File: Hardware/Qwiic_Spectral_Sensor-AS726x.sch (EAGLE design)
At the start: 28 parts, among them J2 Serial Interface, J5 Flash Programming, U1 AS726X, U3 4MB Flash

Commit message: Updated LED
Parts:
- added LOGO2: SFE_LOGO_FLAME.2_INCH, SparkFun-Aesthetics:SFE_LOGO_FLAME.2_INCH
- D2: value 5700k -> White, 60mA; device SparkX:LEDLD -> SparkFun-LED:LED-WHITE3014
- LOGO1: value SFE_LOGO_NAME_FLAME.1_INCH -> SFE_LOGO_FLAME.2_INCH; device SparkFun-Aesthetics:SFE_LOGO_NAME_FLAME.1_INCH -> SparkFun-Aesthetics:SFE_LOGO_FLAME.2_INCH
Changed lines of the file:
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@@
 <layer number="230" name="230bmp" color="7" fill="1" visible="yes" active="yes"/>
 <layer number="231" name="231bmp" color="7" fill="1" visible="yes" active="yes"/>
+<layer number="232" name="Eagle3D_PG2" color="7" fill="1" visible="yes" active="yes"/>
+<layer number="233" name="Eagle3D_PG3" color="7" fill="1" visible="yes" active="yes"/>
 <layer number="248" name="Housing" color="7" fill="1" visible="yes" active="yes"/>
 <layer number="249" name="Edge" color="7" fill="1" visible="yes" active="yes"/>
@@
 <part name="GND8" library="SparkFun-PowerSymbols" deviceset="GND" device=""/>
 <part name="SUPPLY13" library="SparkFun-PowerSymbols" deviceset="3.3V" device=""/>
-<part name="D2" library="SparkX" deviceset="LED" device="LD" value="5700k"/>
+<part name="D2" library="SparkFun-LED" deviceset="LED-WHITE" device="3014" value="White, 60mA"/>
 <part name="J5" library="SparkFun-Connectors" deviceset="AVR_SPI_PROG_3X2" device="TESTPOINTS" value="Flash Programming"/>
 <part name="SUPPLY14" library="SparkFun-PowerSymbols" deviceset="3.3V" device=""/>
@@
 <part name="D4" library="SparkX" deviceset="LED" device="NS" value="Incandescent"/>
 <part name="JP4" library="SparkFun-Jumpers" deviceset="JUMPER-SMT_2_NC_PASTE" device="_NO-SILK" value=""/>
-<part name="LOGO1" library="SparkFun-Aesthetics" deviceset="SFE_LOGO_NAME_FLAME" device=".1_INCH"/>
+<part name="LOGO1" library="SparkFun-Aesthetics" deviceset="SFE_LOGO_FLAME" device=".2_INCH"/>
+<part name="LOGO2" library="SparkFun-Aesthetics" deviceset="SFE_LOGO_FLAME" device=".2_INCH"/>
 </parts>
 <sheets>
@@
 <instance part="GND8" gate="1" x="116.84" y="43.18" rot="MR0"/>
 <instance part="SUPPLY13" gate="G$1" x="116.84" y="58.42" rot="MR0"/>
-<instance part="D2" gate="D1" x="40.64" y="144.78" smashed="yes">
+<instance part="D2" gate="G$1" x="40.64" y="144.78" smashed="yes">
 <attribute name="NAME" x="40.132" y="138.176" size="1.778" layer="95" font="vector" rot="R90"/>
 <attribute name="VALUE" x="42.418" y="139.192" size="1.778" layer="96" font="vector" rot="R90" align="top-left"/>
@@
 </instance>
 <instance part="JP4" gate="G$1" x="40.64" y="154.94" rot="R90"/>
-<instance part="LOGO1" gate="G$1" x="88.9" y="2.54"/>
+<instance part="LOGO1" gate="G$1" x="134.62" y="5.08"/>
+<instance part="LOGO2" gate="G$1" x="134.62" y="5.08"/>
 </instances>
 <busses>
@@
 <wire x1="60.96" y1="132.08" x2="40.64" y2="132.08" width="0.1524" layer="91"/>
 <wire x1="40.64" y1="132.08" x2="40.64" y2="139.7" width="0.1524" layer="91"/>
-<pinref part="D2" gate="D1" pin="C"/>
+<pinref part="D2" gate="G$1" pin="C"/>
 <wire x1="33.02" y1="139.7" x2="33.02" y2="132.08" width="0.1524" layer="91"/>
 <wire x1="33.02" y1="132.08" x2="40.64" y2="132.08" width="0.1524" layer="91"/>
@@
 <net name="N$6" class="0">
 <segment>
-<pinref part="D2" gate="D1" pin="A"/>
+<pinref part="D2" gate="G$1" pin="A"/>
 <pinref part="JP4" gate="G$1" pin="1"/>
 <wire x1="40.64" y1="149.86" x2="40.64" y2="147.32" width="0.1524" layer="91"/>

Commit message: Added LED, I2C connectors to SFE library and changed components in schematic
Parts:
- J1, J4: value (none) -> Qwiic Right Angle; device SparkX:I2C_STANDARDJS-1MM -> SparkFun-Connectors:I2C_STANDARDQWIIC
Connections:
- net 3.3V: now also J1.2, J4.2; no longer J1.VCC, J4.VCC
- net GND: now also J1.1, J4.1; no longer J1.GND, J4.GND
- net RX/SCL: now also J1.4, J4.4; no longer J1.SCL, J4.SCL
- net TX/SDA: now also J1.3, J4.3; no longer J1.SDA, J4.SDA
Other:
- note added: "U1 can be populated with AS7262 or AS7263"
- note removed: "FTDI Port"
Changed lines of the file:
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@@
 <part name="SUPPLY6" library="SparkFun-PowerSymbols" deviceset="3.3V" device=""/>
 <part name="GND5" library="SparkFun-PowerSymbols" deviceset="GND" device=""/>
-<part name="J1" library="SparkX" deviceset="I2C_STANDARD" device="JS-1MM"/>
+<part name="J1" library="SparkFun-Connectors" deviceset="I2C_STANDARD" device="QWIIC" value="Qwiic Right Angle"/>
 <part name="SUPPLY7" library="SparkFun-PowerSymbols" deviceset="3.3V" device=""/>
 <part name="D1" library="SparkFun-LED" deviceset="LED-BLUE" device="0603" value="BLUE"/>
@@
 <part name="SUPPLY3" library="SparkFun-PowerSymbols" deviceset="3.3V" device=""/>
 <part name="GND3" library="SparkFun-PowerSymbols" deviceset="GND" device=""/>
-<part name="J4" library="SparkX" deviceset="I2C_STANDARD" device="JS-1MM"/>
+<part name="J4" library="SparkFun-Connectors" deviceset="I2C_STANDARD" device="QWIIC" value="Qwiic Right Angle"/>
 <part name="GND8" library="SparkFun-PowerSymbols" deviceset="GND" device=""/>
 <part name="SUPPLY13" library="SparkFun-PowerSymbols" deviceset="3.3V" device=""/>
@@
 <text x="10.16" y="116.84" size="1.778" layer="97">CRI: 80</text>
 <text x="48.26" y="81.28" size="1.778" layer="97">7-bit unshifted I2C address: 0x49</text>
-<text x="134.62" y="45.72" size="1.778" layer="91" rot="R90">FTDI Port</text>
-<text x="180.34" y="45.72" size="1.778" layer="91" rot="R90">FTDI Port</text>
 <text x="93.98" y="43.18" size="1.778" layer="91" rot="R90">I2C interface</text>
 <text x="93.98" y="27.94" size="1.778" layer="91" rot="R90">Interrupt/
 Reset</text>
 <text x="148.59" y="7.112" size="2.54" layer="95">Revised by: Andy England</text>
+<text x="48.26" y="106.68" size="1.524" layer="91">U1 can be populated with AS7262 or AS7263</text>
 </plain>
 <instances>
@@
 <instance part="SUPPLY6" gate="G$1" x="205.74" y="152.4"/>
 <instance part="GND5" gate="1" x="170.18" y="137.16"/>
-<instance part="J1" gate="G$1" x="172.72" y="50.8" rot="MR0"/>
+<instance part="J1" gate="G$1" x="172.72" y="50.8" smashed="yes" rot="MR0">
+<attribute name="VALUE" x="180.594" y="63.5" size="1.778" layer="96" font="vector" rot="MR270" align="top-left"/>
+<attribute name="NAME" x="177.8" y="58.674" size="1.778" layer="95" font="vector" rot="MR0"/>
+</instance>
 <instance part="SUPPLY7" gate="G$1" x="170.18" y="152.4"/>
 <instance part="D1" gate="G$1" x="50.8" y="144.78" smashed="yes">
@@
 <instance part="SUPPLY3" gate="G$1" x="215.9" y="63.5" rot="MR0"/>
 <instance part="GND3" gate="1" x="215.9" y="43.18" rot="MR0"/>
-<instance part="J4" gate="G$1" x="127" y="50.8" rot="MR0"/>
+<instance part="J4" gate="G$1" x="127" y="50.8" smashed="yes" rot="MR0">
+<attribute name="VALUE" x="134.874" y="63.5" size="1.778" layer="96" font="vector" rot="MR270" align="top-left"/>
+<attribute name="NAME" x="132.08" y="58.674" size="1.778" layer="95" font="vector" rot="MR0"/>
+</instance>
 <instance part="GND8" gate="1" x="116.84" y="43.18" rot="MR0"/>
 <instance part="SUPPLY13" gate="G$1" x="116.84" y="58.42" rot="MR0"/>
@@
 </segment>
 <segment>
-<pinref part="J1" gate="G$1" pin="GND"/>
+<pinref part="J1" gate="G$1" pin="1"/>
 <wire x1="165.1" y1="48.26" x2="162.56" y2="48.26" width="0.1524" layer="91"/>
 <wire x1="162.56" y1="48.26" x2="162.56" y2="45.72" width="0.1524" layer="91"/>
@@
 </segment>
 <segment>
-<pinref part="J4" gate="G$1" pin="GND"/>
+<pinref part="J4" gate="G$1" pin="1"/>
 <wire x1="119.38" y1="48.26" x2="116.84" y2="48.26" width="0.1524" layer="91"/>
 <wire x1="116.84" y1="48.26" x2="116.84" y2="45.72" width="0.1524" layer="91"/>
@@
 </segment>
 <segment>
-<pinref part="J1" gate="G$1" pin="SCL"/>
+<pinref part="J1" gate="G$1" pin="4"/>
 <wire x1="165.1" y1="55.88" x2="160.02" y2="55.88" width="0.1524" layer="91"/>
 <label x="160.02" y="55.88" size="1.27" layer="95" rot="R180" xref="yes"/>
@@
 </segment>
 <segment>
-<pinref part="J4" gate="G$1" pin="SCL"/>
+<pinref part="J4" gate="G$1" pin="4"/>
 <wire x1="119.38" y1="55.88" x2="114.3" y2="55.88" width="0.1524" layer="91"/>
 <label x="114.3" y="55.88" size="1.27" layer="95" rot="R180" xref="yes"/>
@@
 </segment>
 <segment>
-<pinref part="J1" gate="G$1" pin="SDA"/>
+<pinref part="J1" gate="G$1" pin="3"/>
 <wire x1="165.1" y1="53.34" x2="160.02" y2="53.34" width="0.1524" layer="91"/>
 <label x="160.02" y="53.34" size="1.27" layer="95" rot="R180" xref="yes"/>
@@
 </segment>
 <segment>
-<pinref part="J4" gate="G$1" pin="SDA"/>
+<pinref part="J4" gate="G$1" pin="3"/>
 <wire x1="119.38" y1="53.34" x2="114.3" y2="53.34" width="0.1524" layer="91"/>
 <label x="114.3" y="53.34" size="1.27" layer="95" rot="R180" xref="yes"/>
@@
 </segment>
 <segment>
-<pinref part="J1" gate="G$1" pin="VCC"/>
+<pinref part="J1" gate="G$1" pin="2"/>
 <wire x1="165.1" y1="50.8" x2="162.56" y2="50.8" width="0.1524" layer="91"/>
 <wire x1="162.56" y1="50.8" x2="162.56" y2="58.42" width="0.1524" layer="91"/>
@@
 </segment>
 <segment>
-<pinref part="J4" gate="G$1" pin="VCC"/>
+<pinref part="J4" gate="G$1" pin="2"/>
 <wire x1="119.38" y1="50.8" x2="116.84" y2="50.8" width="0.1524" layer="91"/>
 <wire x1="116.84" y1="50.8" x2="116.84" y2="58.42" width="0.1524" layer="91"/>

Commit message: Updated all schematics to point to proper library
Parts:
- U1: value AS726X -> IR; device SparkX:AS726X -> SparkFun-Sensors:AS726XIR
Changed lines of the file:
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@@
 <part name="FD1" library="SparkFun-Aesthetics" deviceset="FIDUCIAL" device="1X2"/>
 <part name="FD2" library="SparkFun-Aesthetics" deviceset="FIDUCIAL" device="1X2"/>
-<part name="U1" library="SparkX" deviceset="AS726X" device=""/>
+<part name="U1" library="SparkFun-Sensors" deviceset="AS726X" device="IR" value="IR"/>
 <part name="GND2" library="SparkFun-PowerSymbols" deviceset="GND" device=""/>
 <part name="SUPPLY1" library="SparkFun-PowerSymbols" deviceset="3.3V" device=""/>

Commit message: Fixed minor borad layout issues
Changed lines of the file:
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@@
 Reset</text>
 <text x="148.59" y="7.112" size="2.54" layer="95">Revised by: Andy England</text>
-<text x="48.26" y="106.68" size="1.524" layer="91">U1 can be populated with AS7262 or AS7263</text>
+<text x="48.26" y="106.68" size="1.524" layer="97">U1 can be populated with AS7262 or AS7263</text>
 </plain>
 <instances>

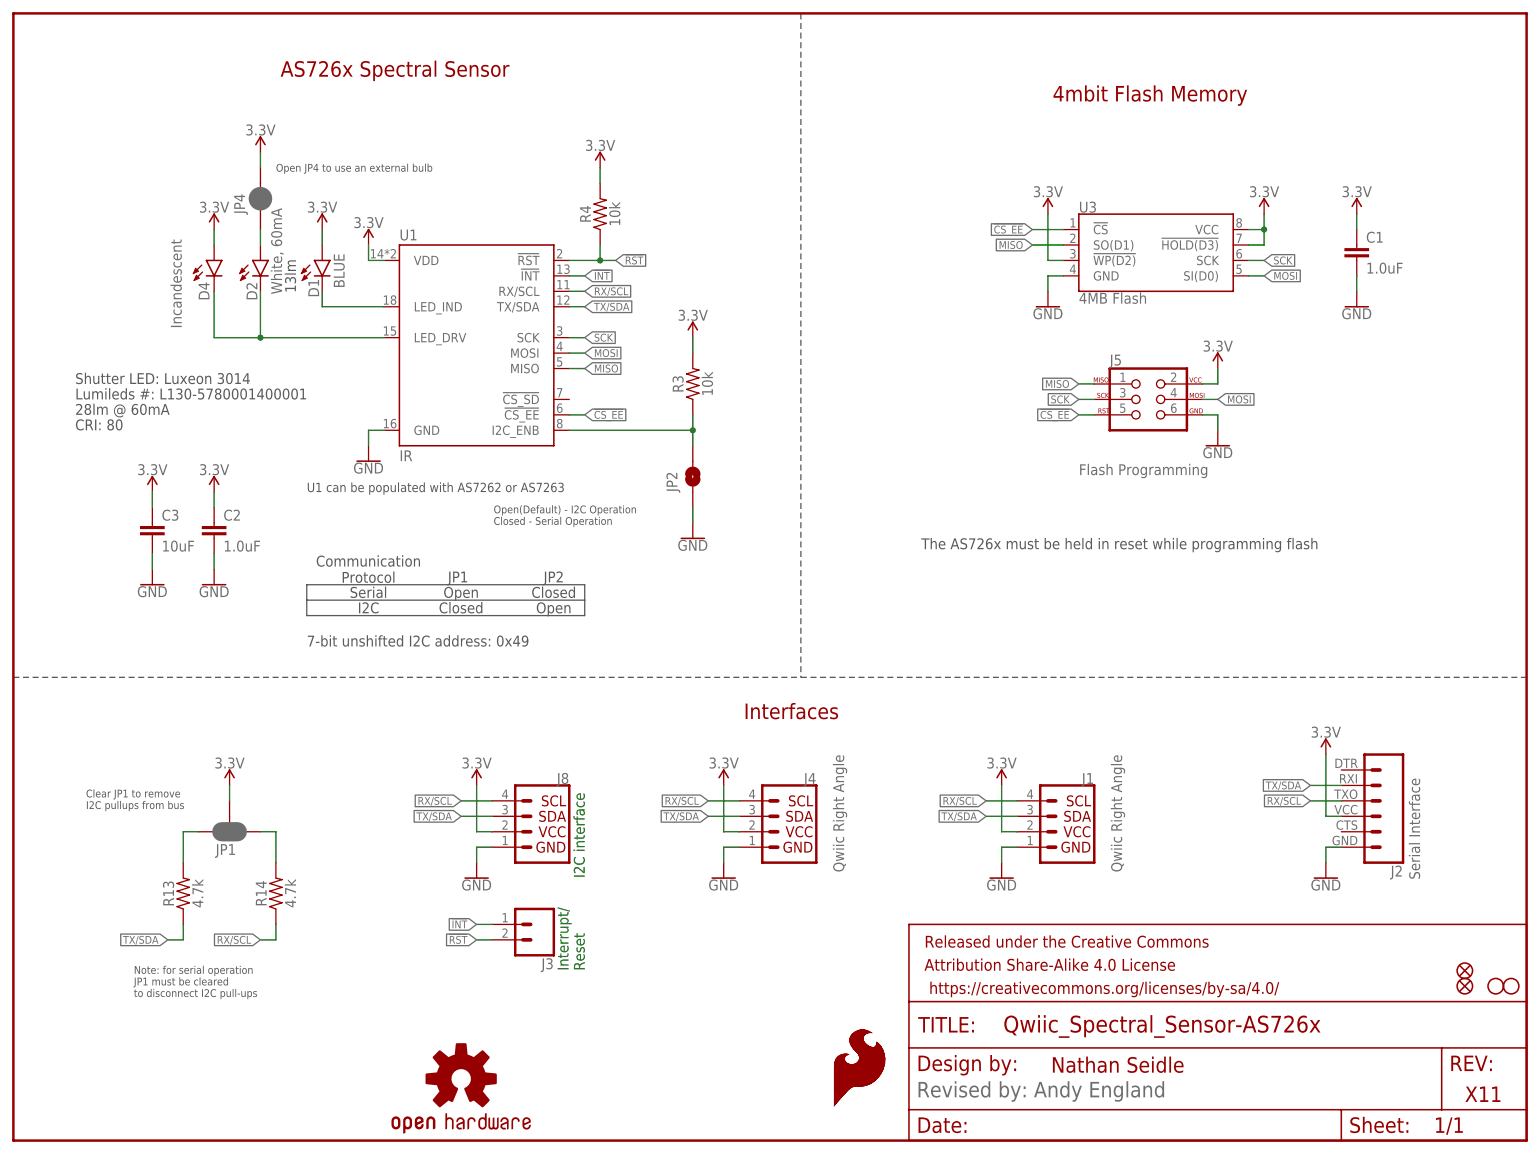
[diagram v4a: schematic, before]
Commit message: Post design review changes. Cream on JP1 and AS726X still needs to be changed
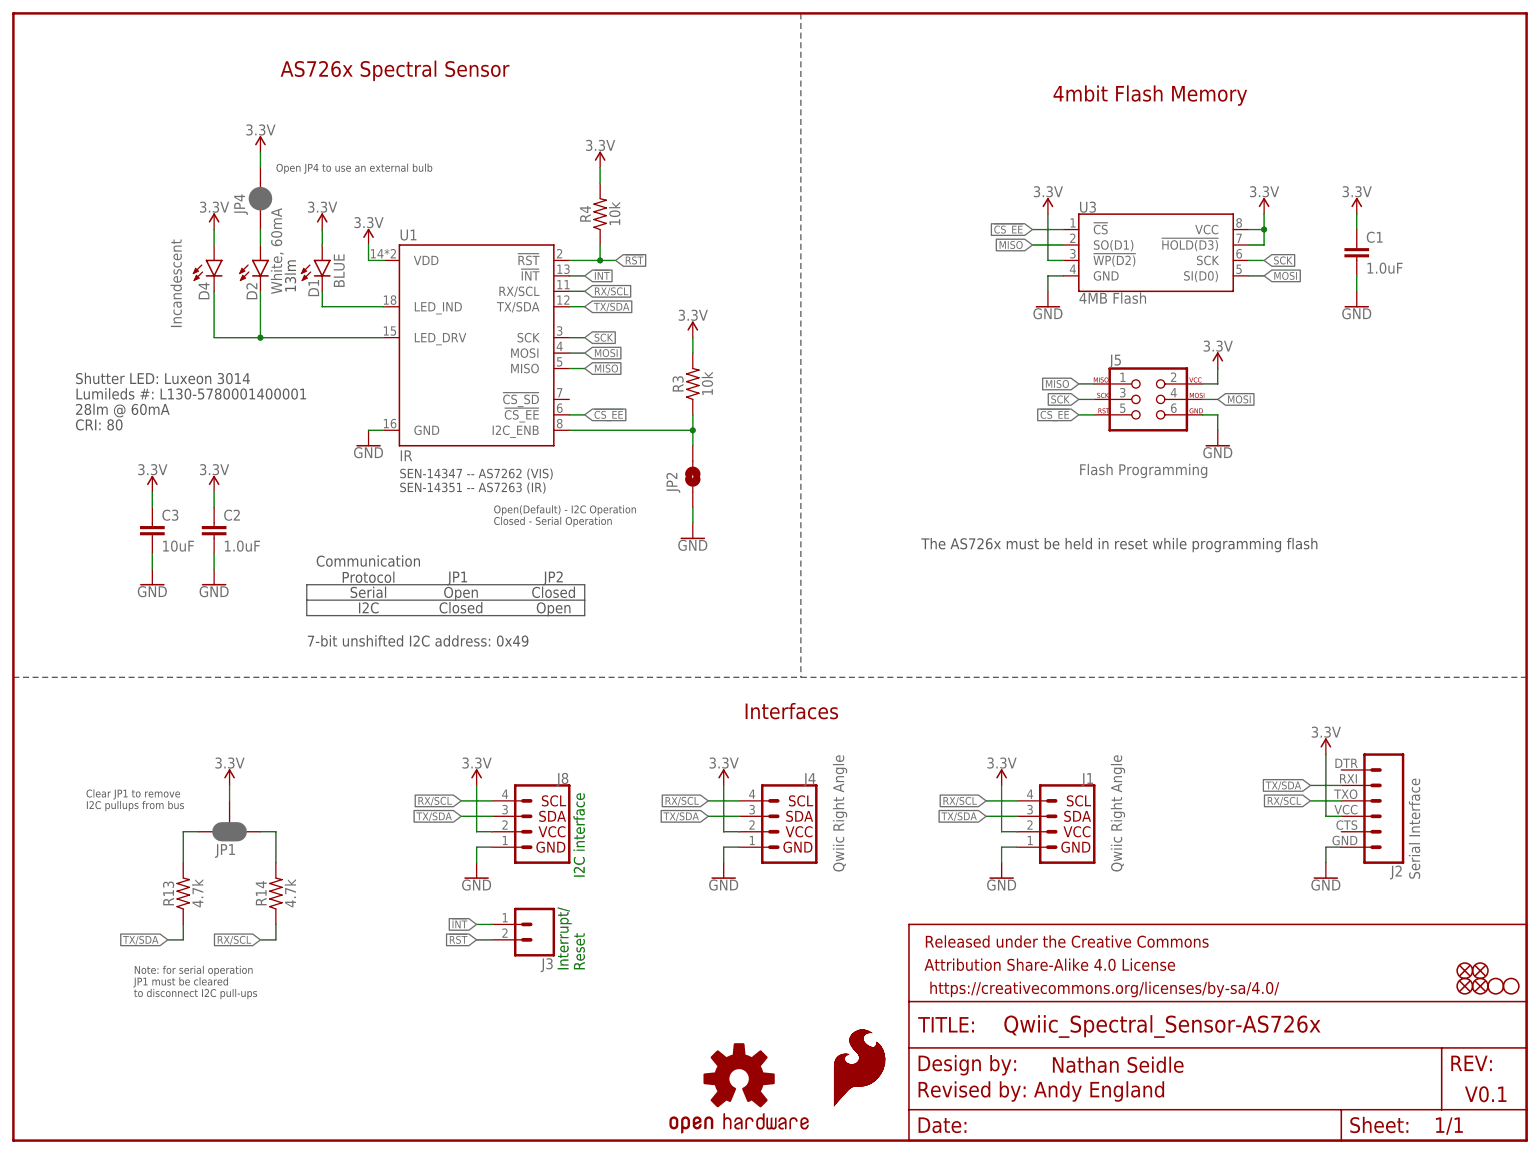
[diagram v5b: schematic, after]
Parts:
- added FD3, FD4: FIDUCIAL1X2, SparkFun-Aesthetics:FIDUCIAL1X2
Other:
- note added: "SEN-14347 -- AS7262 (VIS) SEN-14351 -- AS7263 (IR)"
- note added: "V0.1"
- note removed: "U1 can be populated with AS7262 or AS7263"
- note removed: "X11"
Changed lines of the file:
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@@
 <part name="LOGO1" library="SparkFun-Aesthetics" deviceset="SFE_LOGO_FLAME" device=".2_INCH"/>
 <part name="LOGO2" library="SparkFun-Aesthetics" deviceset="SFE_LOGO_FLAME" device=".2_INCH"/>
+<part name="FD3" library="SparkFun-Aesthetics" deviceset="FIDUCIAL" device="1X2"/>
+<part name="FD4" library="SparkFun-Aesthetics" deviceset="FIDUCIAL" device="1X2"/>
 </parts>
 <sheets>
@@
 <text x="11.938" y="56.134" size="1.27" layer="97" rot="R180" align="center-right">Clear JP1 to remove
 I2C pullups from bus</text>
-<text x="238.76" y="7.62" size="2.54" layer="94" align="center-left">X11</text>
+<text x="238.76" y="7.62" size="2.54" layer="94" align="center-left">V0.1</text>
 <text x="170.688" y="12.446" size="2.54" layer="94" align="center-left">Nathan Seidle</text>
 <wire x1="0" y1="76.2" x2="129.54" y2="76.2" width="0.2032" layer="97" style="longdash"/>
@@
 <text x="93.98" y="27.94" size="1.778" layer="91" rot="R90">Interrupt/
 Reset</text>
-<text x="148.59" y="7.112" size="2.54" layer="95">Revised by: Andy England</text>
-<text x="48.26" y="106.68" size="1.524" layer="97">U1 can be populated with AS7262 or AS7263</text>
+<text x="148.59" y="7.112" size="2.54" layer="94">Revised by: Andy England</text>
+<text x="63.5" y="106.68" size="1.524" layer="97">SEN-14347 -- AS7262 (VIS)
+SEN-14351 -- AS7263 (IR)</text>
 </plain>
 <instances>
@@
 <attribute name="VALUE" x="35.179" y="48.26" size="1.778" layer="96" font="vector" rot="R270" align="top-left"/>
 </instance>
-<instance part="LOGO4" gate="G$1" x="73.66" y="10.16"/>
+<instance part="LOGO4" gate="G$1" x="119.38" y="10.16"/>
 <instance part="FD1" gate="G$1" x="238.76" y="25.4"/>
 <instance part="FD2" gate="G$1" x="238.76" y="27.94"/>
 <instance part="U1" gate="U1" x="76.2" y="129.54"/>
-<instance part="GND2" gate="1" x="58.42" y="111.76"/>
+<instance part="GND2" gate="1" x="58.42" y="114.3"/>
 <instance part="SUPPLY1" gate="G$1" x="58.42" y="147.32"/>
 <instance part="R3" gate="G$1" x="111.76" y="124.46" rot="R90"/>
@@
 <instance part="LOGO1" gate="G$1" x="134.62" y="5.08"/>
 <instance part="LOGO2" gate="G$1" x="134.62" y="5.08"/>
+<instance part="FD3" gate="G$1" x="241.3" y="27.94"/>
+<instance part="FD4" gate="G$1" x="241.3" y="25.4"/>
 </instances>
 <busses>
@@
 <pinref part="U1" gate="U1" pin="GND"/>
 <wire x1="60.96" y1="116.84" x2="58.42" y2="116.84" width="0.1524" layer="91"/>
-<wire x1="58.42" y1="116.84" x2="58.42" y2="114.3" width="0.1524" layer="91"/>
 <pinref part="GND2" gate="1" pin="GND"/>
 </segment>
